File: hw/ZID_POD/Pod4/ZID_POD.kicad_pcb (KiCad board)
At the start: 2 copper layers, 52.8 x 19.3 mm, 2 parts, among them J1 Z80-POD

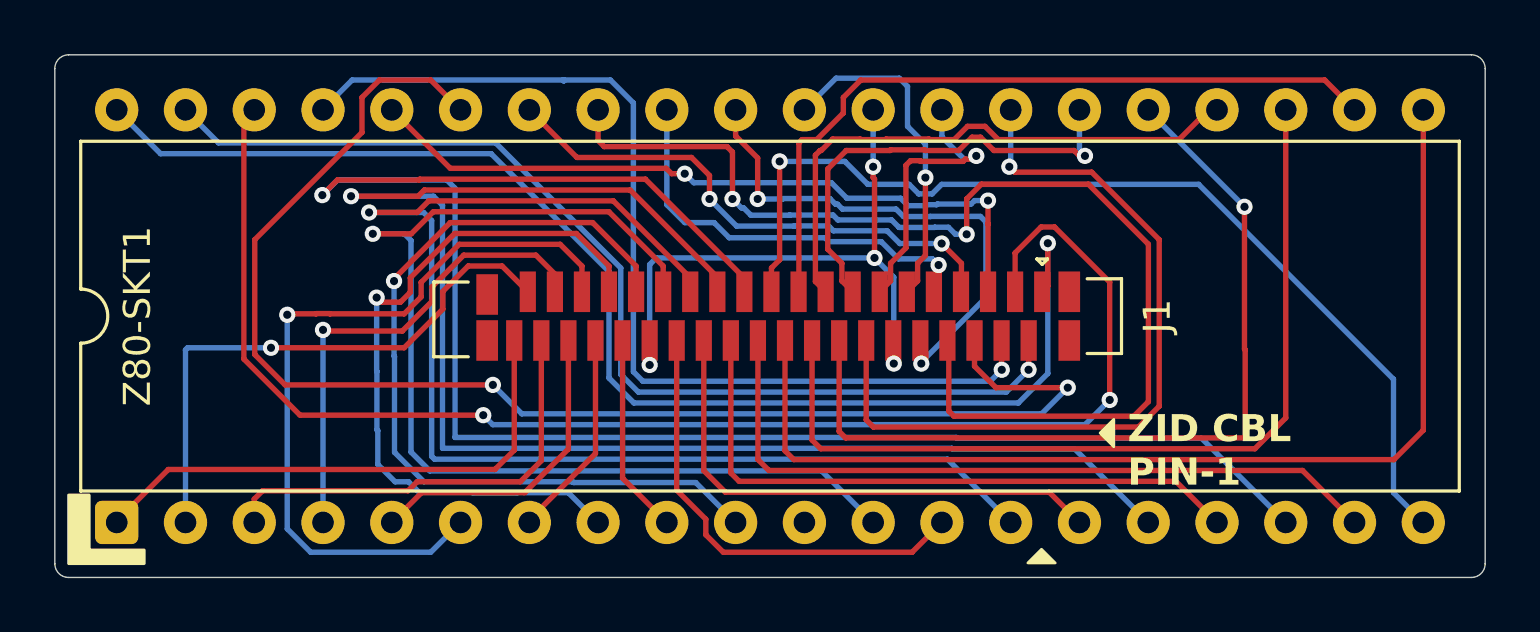
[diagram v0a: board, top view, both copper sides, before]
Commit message: POD PCB increase GND trace width
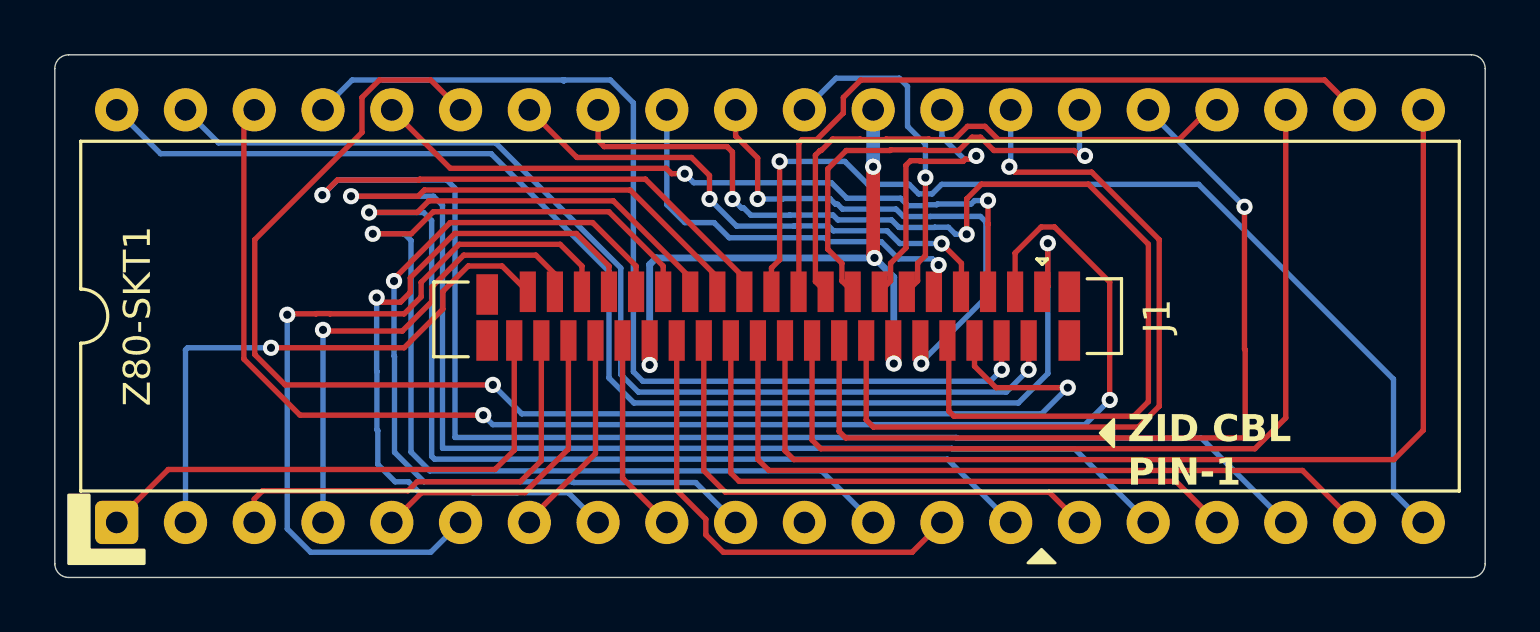
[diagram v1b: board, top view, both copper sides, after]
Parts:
- J1: value Z80-POD -> Z80-POD (4)
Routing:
- net /A8: track 53.2 -> 52.7 mm
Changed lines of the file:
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@@
 	)
 	(setup
+		(stackup
+			(layer "F.SilkS"
+				(type "Top Silk Screen")
+			)
+			(layer "F.Paste"
+				(type "Top Solder Paste")
+			)
+			(layer "F.Mask"
+				(type "Top Solder Mask")
+				(thickness 0.01)
+			)
+			(layer "F.Cu"
+				(type "copper")
+				(thickness 0.035)
+			)
+			(layer "dielectric 1"
+				(type "core")
+				(thickness 1.51)
+				(material "FR4")
+				(epsilon_r 4.5)
+				(loss_tangent 0.02)
+			)
+			(layer "B.Cu"
+				(type "copper")
+				(thickness 0.035)
+			)
+			(layer "B.Mask"
+				(type "Bottom Solder Mask")
+				(thickness 0.01)
+			)
+			(layer "B.Paste"
+				(type "Bottom Solder Paste")
+			)
+			(layer "B.SilkS"
+				(type "Bottom Silk Screen")
+			)
+			(copper_finish "None")
+			(dielectric_constraints no)
+		)
 		(pad_to_mask_clearance 0)
 		(allow_soldermask_bridges_in_footprints no)
@@
 			)
 		)
-		(property "Value" "Z80-POD"
-			(at 0 14 90)
-			(layer "F.Fab")
+		(property "Value" "Z80-POD (4)"
+			(at 0 14 0)
+			(unlocked yes)
+			(layer "B.SilkS")
 			(effects
 				(font
@@
 					(thickness 0.15)
 				)
+				(justify mirror)
 			)
 		)
@@
 	)
 	(segment
-		(start 120.142 96.737)
-		(end 120.1928 96.7878)
-		(width 0.2)
-		(layer "F.Cu")
-		(net 3)
-	)
-	(segment
 		(start 120.904 103.6066)
 		(end 120.886 103.5886)
-		(width 0.2)
-		(layer "F.Cu")
-		(net 3)
-	)
-	(segment
-		(start 120.1928 96.7878)
-		(end 120.1928 99.703998)
-		(width 0.2)
-		(layer "F.Cu")
-		(net 3)
-	)
-	(segment
-		(start 120.142 96.336)
-		(end 120.142 96.737)
-		(width 0.2)
+		(width 0.254)
 		(layer "F.Cu")
 		(net 3)
@@
 		(start 111.887 103.6574)
 		(end 111.887 102.755)
-		(width 0.2)
+		(width 0.254)
 		(layer "F.Cu")
 		(net 3)
@@
 		(start 120.886 103.5886)
 		(end 120.886 102.754)
-		(width 0.2)
+		(width 0.254)
+		(layer "F.Cu")
+		(net 3)
+	)
+	(segment
+		(start 120.142 99.653198)
+		(end 120.1928 99.703998)
+		(width 0.254)
+		(layer "F.Cu")
+		(net 3)
+	)
+	(segment
+		(start 120.142 96.336)
+		(end 120.142 99.653198)
+		(width 0.508)
 		(layer "F.Cu")
 		(net 3)
@@
 		(start 111.887 99.949)
 		(end 112.132002 99.703998)
-		(width 0.2)
+		(width 0.254)
 		(layer "B.Cu")
 		(net 3)
@@
 		(start 120.904 103.6066)
 		(end 120.904 100.415198)
-		(width 0.2)
+		(width 0.254)
 		(layer "B.Cu")
 		(net 3)
@@
 		(start 120.904 100.415198)
 		(end 120.1928 99.703998)
-		(width 0.2)
+		(width 0.254)
 		(layer "B.Cu")
 		(net 3)
@@
 		(start 112.132002 99.703998)
 		(end 120.1928 99.703998)
-		(width 0.2)
+		(width 0.254)
 		(layer "B.Cu")
 		(net 3)
@@
 		(start 120.142 96.336)
 		(end 120.142 94.234)
-		(width 0.2)
+		(width 0.508)
 		(layer "B.Cu")
 		(net 3)
@@
 		(start 111.887 103.6574)
 		(end 111.887 99.949)
-		(width 0.2)
+		(width 0.254)
 		(layer "B.Cu")
 		(net 3)
@@
 	)
 	(segment
-		(start 99.822 94.2086)
-		(end 99.822 94.234)
-		(width 0.2)
-		(layer "B.Cu")
-		(net 9)
-	)
-	(segment
 		(start 108.7485 93.133)
 		(end 108.71315 93.16835)
@@
 		(width 0.2)
 		(layer "F.Cu")
-		(net 14)
-	)
-	(segment
-		(start 96.8992 94.6168)
-		(end 97.282 94.234)
-		(width 0.2)
-		(layer "F.Cu")
